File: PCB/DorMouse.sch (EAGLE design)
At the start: 46 parts, among them IC1 LM340MP-05, IC2 MAX1551, U1 STM32F10XRXT6, X1 MINI-USB-UX60-MB-5ST

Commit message: V1.1 Schematic update
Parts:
- removed JMP1, JMP2: 0R-JUMPA, jump-0r-smd:0R-JUMPA
- removed PAD1, PAD2, PAD3, PAD4: (no value), wirepad:SMD2
- added C21, C23, C24, C25: 0.1uF, rcl:C-EUC0402
- added CHRG: (no value), led:LEDCHIPLED_0603
- added GPS-LED, SD-LED, U$4: RED-GREEN_LED, DorMouse:RED-GREEN_LED
- added R10, R11, R12, R13, R14, R6, R9: 160, rcl:R-EU_R0402
- added R7: 10k, rcl:R-EU_R0402
- added S1, S2: (no value), SparkFun:TAC_SWITCHSMD
- BAROMETER: device DorMouse:MPL115A1 -> Swallow:MPL115A1
- C10: value 10nF -> 1uF
- C11: value 1uF -> 0.01uF
- C12, C7: value 0.1uF -> 0.01uF
- C13: value 0.1uF -> 10nF
- C14, C4: value 0.1uF -> 1uF
- GPS: device DorMouse:UBLOX_MAX-6 -> Swallow:UBLOX_MAX-6
- HIGH-G_ACC: device DorMouse:ADXL377 -> Swallow:ADXL377
- LOW-G_ACC: device DorMouse:ADXL345 -> Swallow:ADXL345
- XB1: device DorMouse:XBEE -> Swallow:XBEE
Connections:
- removed net AVR-INT0: GPS.4_TIMEPULSE
- removed net N$13: JMP2-0R.3, R4.1
- removed net N$22: JTAG1.7
- removed net N$25: JTAG1.9
- removed net U1-CTS: FTDI-HEADER.6, JMP1-0R.1
- removed net U1-RTS: FTDI-HEADER.2, JMP2-0R.1
- new net GENERAL_HAPPY_FACE: R14.2, U1PORTC_L.PC7
- new net GPS_:(: R9.2, U1PORTC_L.PC4
- new net GPS_:): R10.2, U1PORTC_L.PC3
- new net MISO-3: U1PORTB_L.PB4
- new net MOSI-3: U1PORTB_L.PB5
- new net N$17: GPS-LED.RED-ANODE, R9.1
- new net N$19: C10.1, FTDI-HEADER.6
- new net N$21: R7.2, U1PORTB_H.PB9
- new net N$27: GPS-LED.GREEN-ANODE, R10.1
- new net N$30: R11.1, SD-LED.RED-ANODE
- new net N$31: R12.1, SD-LED.GREEN-ANODE
- new net N$33: R13.1, U$4.RED-ANODE
- new net N$34: R14.1, U$4.GREEN-ANODE
- new net RESET: C10.2, C6.2, S2.1, S2.2, U1RESET.NRST
- new net SCK-3: U1PORTB_L.PB3
- new net SD-DET: CN1.CARD_DETECT, U1PORTC_H.PC13
- new net SD_:(: R11.2, U1PORTC_L.PC6
- new net SD_:): R12.2, U1PORTC_L.PC5
- new net SERGEANT_SAD_FACE: R13.2, U1PORTA_H.PA8
- new net TIMEPULSE: GPS.4_TIMEPULSE, U1PORTB_H.PB8
- net ADC1: now also C7.1
- net ADC2: now also C11.1
- net ADC3: now also C12.1
- net CHARGING(-): now also U1PORTA_L.PA0
- net GND: now also C12.2, C13.2, C14.2, C21.1, C23.1, C24.1, C25.1, C7.2, CN1.CARD_DETECT1, FTDI-HEADER.2, GPS-LED.CATHODE, JTAG1.9, R6.1, S2.3, S2.4, SD-LED.CATHODE, U$4.CATHODE, U1AN_POWER.VDDA; no longer C10.2, C12.1, C13.1, C14.1, PAD4.P, U1AN_POWER.VSSA
- net N$12: now also CHRG.C, R6.2; no longer JMP1-0R.3, R3.1
- net N$2: now also S1.3, S1.4; no longer PAD2.P
- net N$5: now also R3.1; no longer JMP1-0R.2
- net N$8: now also R4.1; no longer JMP2-0R.2
- net N$9: now also CHRG.A, U1PORTA_L.PA1; no longer C6.2, PAD3.P, U1RESET.NRST
- net TCK: no longer U1PORTA_H.PA14
- net TDI: no longer U1PORTA_H.PA15
- net TDO: no longer U1PORTB_L.PB3
- net TMS: no longer U1PORTA_H.PA13
- net USB-5V: now also R7.1
- net VCC: now also C13.1, C14.1, C21.2, C23.2, C24.2, C25.2, S1.1, S1.2, U1AN_POWER.VSSA; no longer C10.1, C11.1, C12.2, C13.2, C14.2, PAD1.P, U1AN_POWER.VDDA
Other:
- moved on the sheet: C10, C11, C12, C13, C14, C15, C16, C17, C18, C19, C20, C22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

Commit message: pcb v1
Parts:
- removed C13: 10nF, rcl:C-EUC0402
- removed C17, C20, C5: 0.1uF, rcl:C-EUC0402
- removed C4: 1uF, rcl:C-EUC0402
- added CN2: (no value), microbuilder:JST_2PINSH2
- renumbered U$4 to GENERAL
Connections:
- removed net NRESET: JTAG1.10
- removed net SCK-3: U1PORTB_L.PB3
- net GND: now also CN2.1; no longer C13.2, C17.1, C20.1, C4.1, C5.2
- net LIPO+: now also CN2.2; no longer C5.1
- net RESET: now also JTAG1.10
- net TCK: now also U1PORTA_H.PA14
- net TDI: now also U1PORTA_H.PA15
- net TDO: now also U1PORTB_L.PB3
- net TMS: now also U1PORTA_H.PA13
- net VCC: no longer C13.1, C17.2, C20.2, C4.2

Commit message: Multiple fixes to schematic, addition of pdf, clean board and partslist.
Ava library fixed: open and save, then it works (?)

Ran ERC: complained about missing joins and signals near each other without
being connected. Discovered one case where something that should be
conected was not. Fixed, then as a precautionary measure, added join
dots everywhere (sorry).

Wrong antenna footprint. Swapped.

Adam says the two-capacitors-with-different-values thing is to do with
response to different frequencies. Added datasheet recommended capacitor
values for the STM analogue.

Adjusted capacitor count for low g accel.

Add parts list
Add schematic PDF
Add 'clean, with groups of easy things routed' board.

Warning: I (foolishly) did the schematic modifications with the clean
board open. This de-synced the board, so I manually re synced them
afterwards, and eagle is now content. Hopefully crazy rubbish won't
happen.
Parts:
- removed C15: 0.1uF, rcl:C-EUC0402
- added C4: 10nF, rcl:C-EUC0402
- added C5: 4.7uF, rcl:C-EUC0402
- GPS: device Swallow:UBLOX_MAX-6 -> Ava:UBLOX_MAX-6
- U$1: value SARANTEL-SL1204 -> SARANTEL-SR1202; device Swallow:SARANTEL-SL1204 -> Ava:SARANTEL-SR1202
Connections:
- net GND: now also C4.2, C5.1, U1AN_POWER.VSSA; no longer C15.1, U1AN_POWER.VDDA
- net VCC: now also C4.1, C5.2, U1AN_POWER.VDDA; no longer C15.2, U1AN_POWER.VSSA
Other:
- moved on the sheet: C14, C16, C18, C19, C22, U1AN_POWER

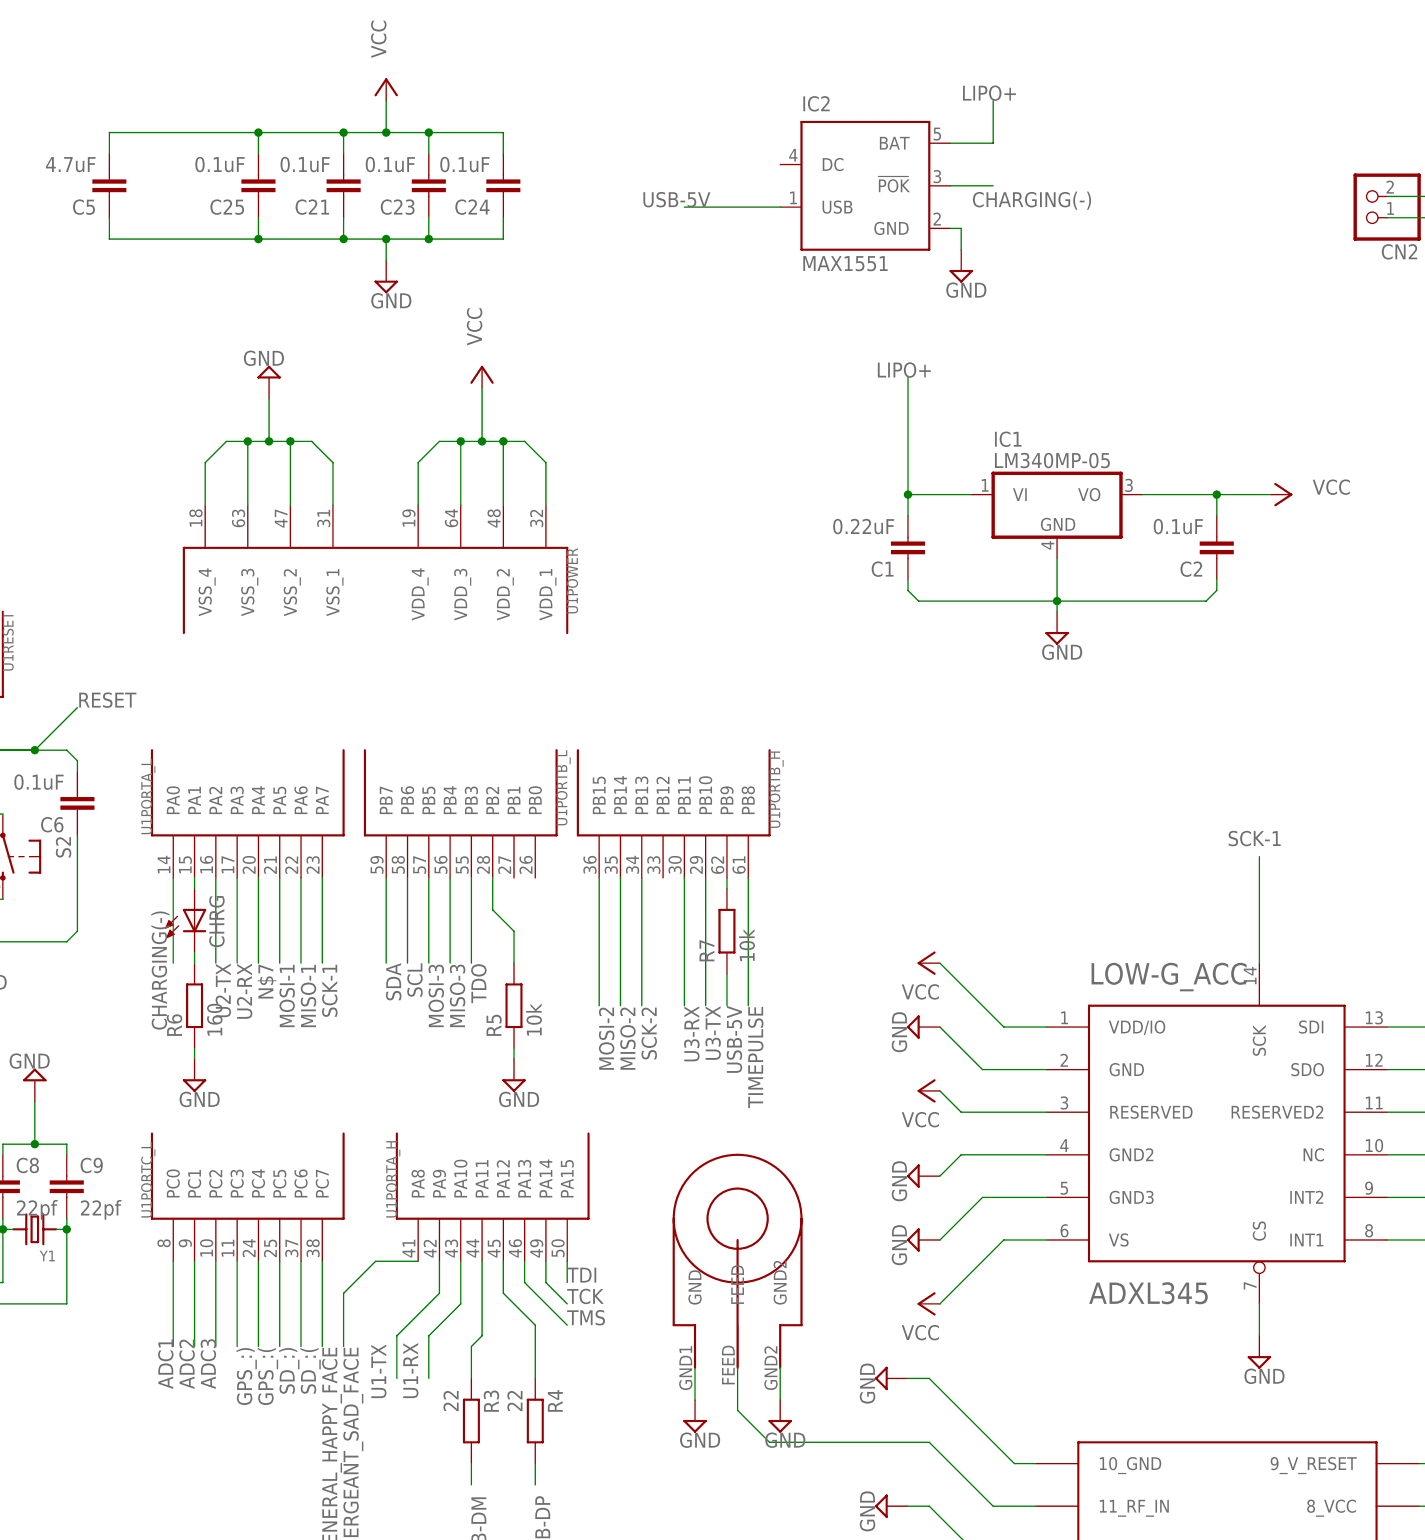
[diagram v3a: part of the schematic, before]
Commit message: Add resistor and cap, reverse ADC connections. Warning: desync
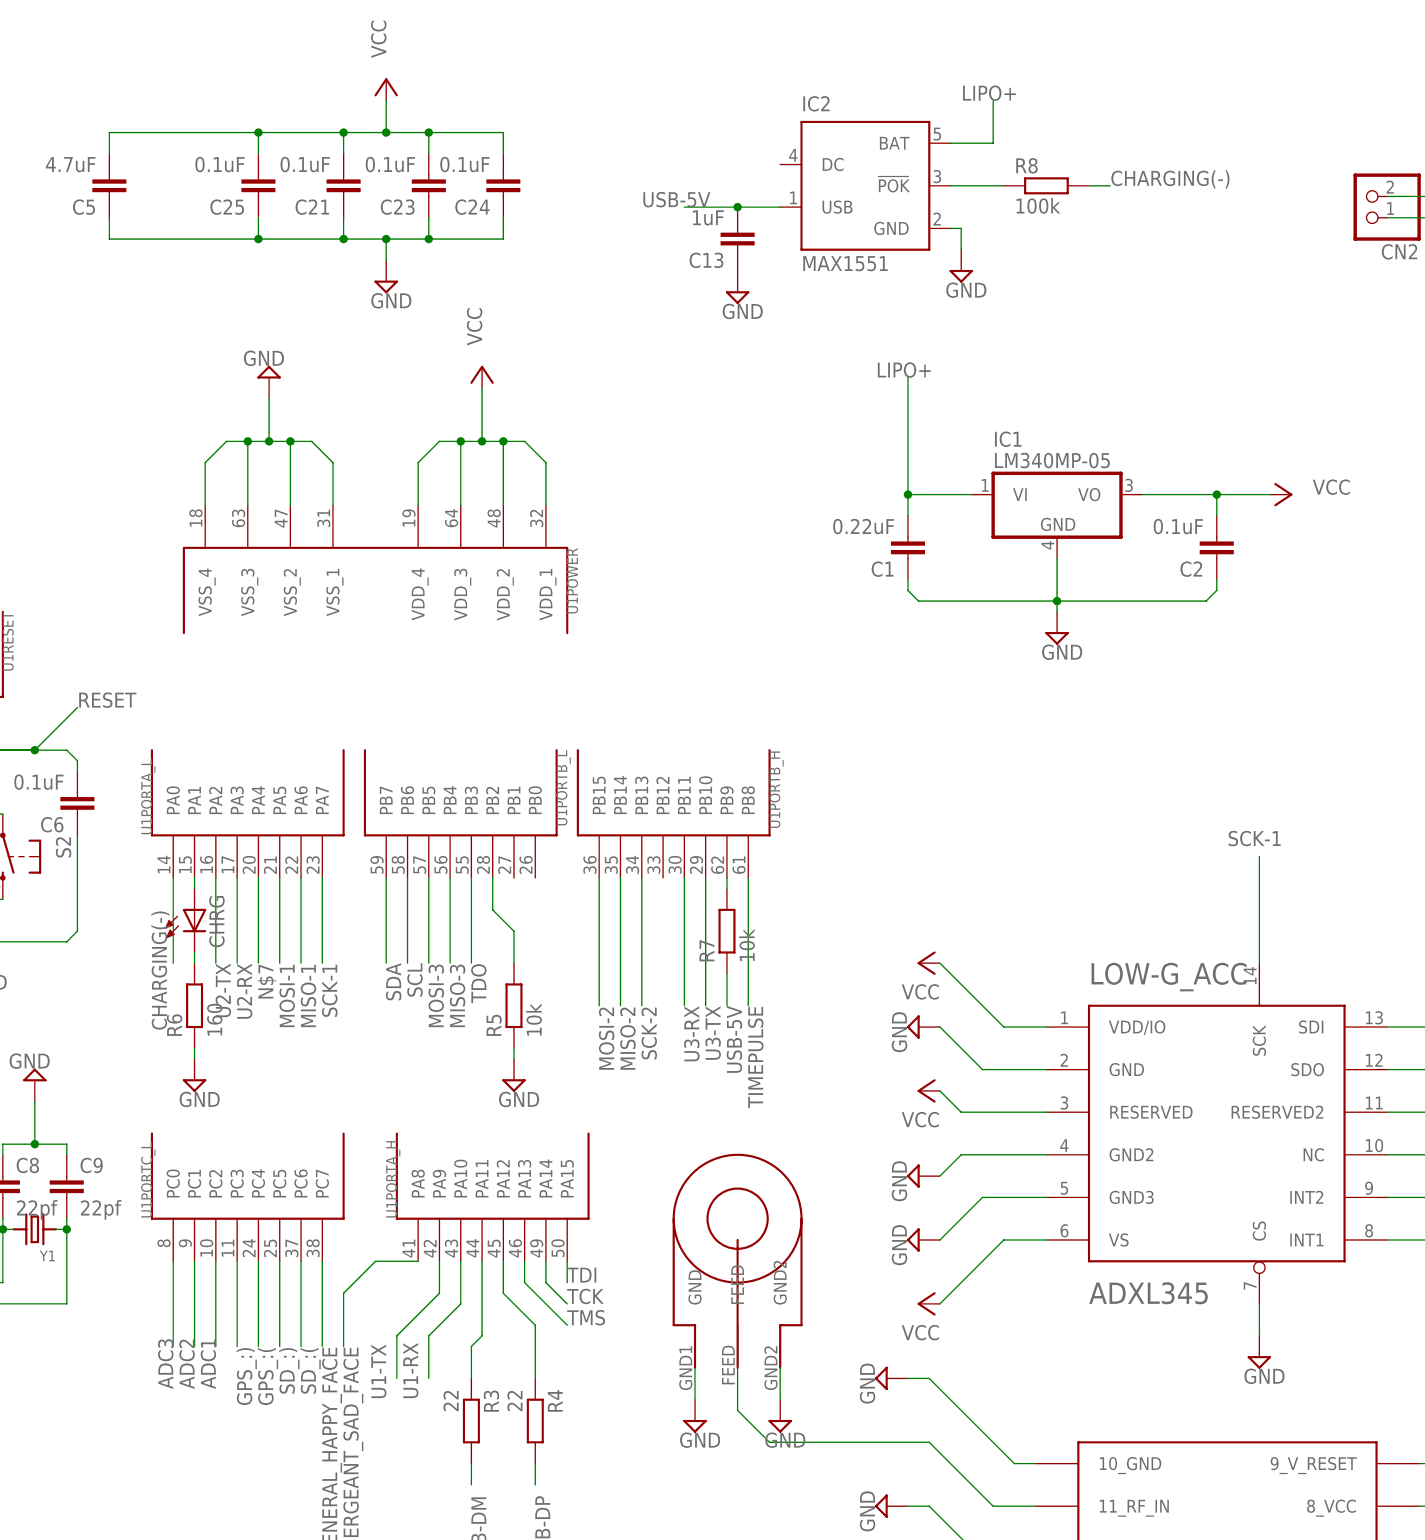
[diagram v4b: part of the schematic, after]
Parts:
- added C13: 1uF, rcl:C-EUC0402
- added R8: 100k, rcl:R-EU_R0402
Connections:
- new net N$13: IC2.!POK, R8.1
- net ADC1: now also U1PORTC_L.PC2; no longer U1PORTC_L.PC0
- net ADC3: now also U1PORTC_L.PC0; no longer U1PORTC_L.PC2
- net CHARGING(-): now also R8.2; no longer IC2.!POK
- net GND: now also C13.1
- net USB-5V: now also C13.2
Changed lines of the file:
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@@
 <part name="C4" library="rcl" deviceset="C-EU" device="C0402" value="10nF"/>
 <part name="C5" library="rcl" deviceset="C-EU" device="C0402" value="4.7uF"/>
+<part name="C13" library="rcl" deviceset="C-EU" device="C0402" value="1uF"/>
+<part name="SUPPLY11" library="supply2" deviceset="GND" device=""/>
+<part name="R8" library="rcl" deviceset="R-EU_" device="R0402" value="100k"/>
 </parts>
 <sheets>
@@
 <instance part="C4" gate="G$1" x="-168.91" y="80.01" rot="R180"/>
 <instance part="C5" gate="G$1" x="-85.09" y="121.92" rot="R180"/>
+<instance part="C13" gate="G$1" x="-10.16" y="115.57" rot="R180"/>
+<instance part="SUPPLY11" gate="GND" x="-10.16" y="110.49"/>
+<instance part="R8" gate="G$1" x="26.67" y="123.19"/>
 </instances>
 <busses>
@@
 <pinref part="SUPPLY41" gate="GND" pin="GND"/>
 </segment>
+<segment>
+<pinref part="C13" gate="G$1" pin="1"/>
+<pinref part="SUPPLY11" gate="GND" pin="GND"/>
+</segment>
 </net>
 <net name="VCC" class="0">
@@
 <segment>
 <pinref part="IC2" gate="G$1" pin="USB"/>
-<wire x1="-5.08" y1="120.65" x2="-16.51" y2="120.65" width="0.1524" layer="91"/>
+<wire x1="-5.08" y1="120.65" x2="-10.16" y2="120.65" width="0.1524" layer="91"/>
 <label x="-21.59" y="120.65" size="1.778" layer="95"/>
+<pinref part="C13" gate="G$1" pin="2"/>
+<wire x1="-10.16" y1="120.65" x2="-16.51" y2="120.65" width="0.1524" layer="91"/>
+<junction x="-10.16" y="120.65"/>
 </segment>
 <segment>
@@
 <net name="CHARGING(-)" class="0">
 <segment>
-<pinref part="IC2" gate="G$1" pin="!POK"/>
-<wire x1="15.24" y1="123.19" x2="20.32" y2="123.19" width="0.1524" layer="91"/>
-<label x="17.78" y="120.65" size="1.778" layer="95"/>
-</segment>
-<segment>
 <pinref part="U1" gate="PORTA_L" pin="PA0"/>
 <wire x1="-77.47" y1="40.64" x2="-77.47" y2="30.48" width="0.1524" layer="91"/>
 <label x="-80.01" y="36.83" size="1.778" layer="95" rot="R270"/>
+</segment>
+<segment>
+<pinref part="R8" gate="G$1" pin="2"/>
+<wire x1="31.75" y1="123.19" x2="34.29" y2="123.19" width="0.1524" layer="91"/>
+<label x="34.29" y="123.19" size="1.778" layer="95"/>
 </segment>
 </net>
@@
 <net name="ADC1" class="0">
 <segment>
-<wire x1="-77.47" y1="-5.08" x2="-77.47" y2="-15.24" width="0.1524" layer="91"/>
-<pinref part="U1" gate="PORTC_L" pin="PC0"/>
-<label x="-77.47" y="-20.32" size="1.778" layer="95" rot="R90"/>
-</segment>
-<segment>
 <pinref part="HIGH-G_ACC" gate="G$1" pin="Z_OUT"/>
 <wire x1="158.75" y1="25.4" x2="172.72" y2="25.4" width="0.1524" layer="91"/>
@@
 <pinref part="C7" gate="G$1" pin="1"/>
 </segment>
+<segment>
+<pinref part="U1" gate="PORTC_L" pin="PC2"/>
+<wire x1="-72.39" y1="-5.08" x2="-72.39" y2="-15.24" width="0.1524" layer="91"/>
+<label x="-72.39" y="-20.32" size="1.778" layer="95" rot="R90"/>
+</segment>
 </net>
 <net name="ADC2" class="0">
-<segment>
-<pinref part="U1" gate="PORTC_L" pin="PC1"/>
-<wire x1="-74.93" y1="-5.08" x2="-74.93" y2="-15.24" width="0.1524" layer="91"/>
-<label x="-74.93" y="-20.32" size="1.778" layer="95" rot="R90"/>
-</segment>
 <segment>
 <pinref part="HIGH-G_ACC" gate="G$1" pin="Y_OUT"/>
@@
 <pinref part="C11" gate="G$1" pin="1"/>
 </segment>
+<segment>
+<pinref part="U1" gate="PORTC_L" pin="PC1"/>
+<wire x1="-74.93" y1="-5.08" x2="-74.93" y2="-15.24" width="0.1524" layer="91"/>
+<label x="-74.93" y="-20.32" size="1.778" layer="95" rot="R90"/>
+</segment>
 </net>
 <net name="ADC3" class="0">
-<segment>
-<pinref part="U1" gate="PORTC_L" pin="PC2"/>
-<wire x1="-72.39" y1="-5.08" x2="-72.39" y2="-15.24" width="0.1524" layer="91"/>
-<label x="-72.39" y="-20.32" size="1.778" layer="95" rot="R90"/>
-</segment>
 <segment>
 <pinref part="HIGH-G_ACC" gate="G$1" pin="X_OUT"/>
@@
 <label x="165.1" y="15.24" size="1.778" layer="95"/>
 <pinref part="C12" gate="G$1" pin="1"/>
+</segment>
+<segment>
+<wire x1="-77.47" y1="-5.08" x2="-77.47" y2="-15.24" width="0.1524" layer="91"/>
+<pinref part="U1" gate="PORTC_L" pin="PC0"/>
+<label x="-77.47" y="-20.32" size="1.778" layer="95" rot="R90"/>
 </segment>
 </net>
@@
 </segment>
 </net>
+<net name="N$13" class="0">
+<segment>
+<pinref part="IC2" gate="G$1" pin="!POK"/>
+<pinref part="R8" gate="G$1" pin="1"/>
+<wire x1="21.59" y1="123.19" x2="15.24" y2="123.19" width="0.1524" layer="91"/>
+</segment>
+</net>

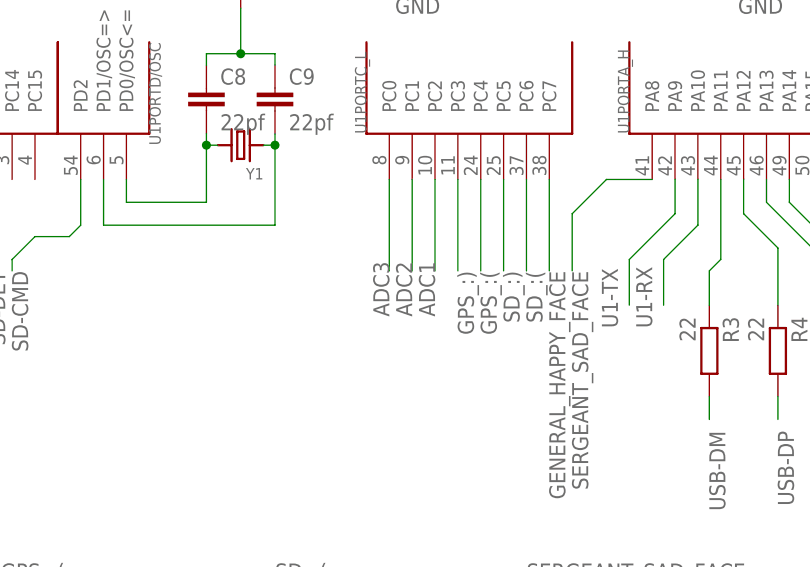
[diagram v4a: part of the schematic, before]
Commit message: Sync older board with schematic
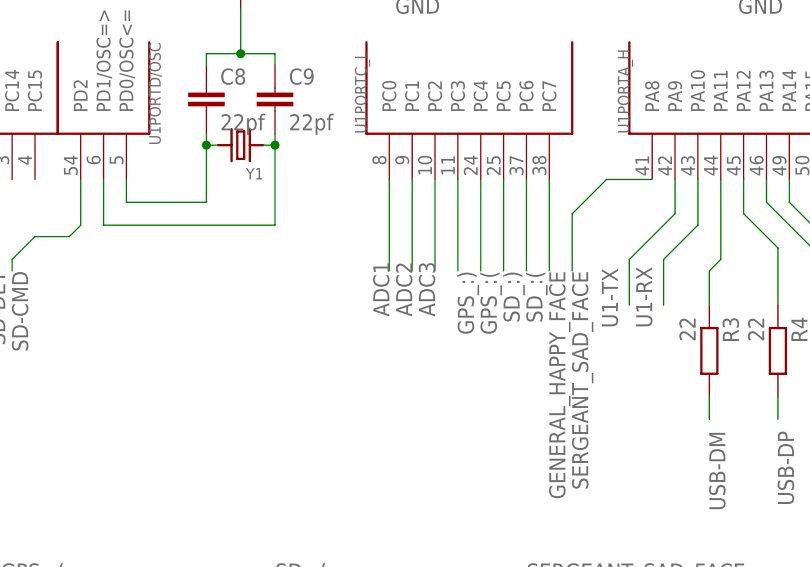
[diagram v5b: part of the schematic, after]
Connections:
- net ADC1: now also U1PORTC_L.PC0; no longer U1PORTC_L.PC2
- net ADC3: now also U1PORTC_L.PC2; no longer U1PORTC_L.PC0
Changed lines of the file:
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@@
 <setting verticaltext="up"/>
 </settings>
-<grid distance="0.05" unitdist="inch" unit="inch" style="lines" multiple="1" display="no" altdistance="0.01" altunitdist="inch" altunit="inch"/>
+<grid distance="0.1" unitdist="inch" unit="inch" style="lines" multiple="1" display="no" altdistance="0.01" altunitdist="inch" altunit="inch"/>
 <layers>
 <layer number="1" name="Top" color="4" fill="1" visible="no" active="no"/>
@@
 </segment>
 <segment>
-<pinref part="U1" gate="PORTC_L" pin="PC2"/>
-<wire x1="-72.39" y1="-5.08" x2="-72.39" y2="-15.24" width="0.1524" layer="91"/>
-<label x="-72.39" y="-20.32" size="1.778" layer="95" rot="R90"/>
+<wire x1="-77.47" y1="-5.08" x2="-77.47" y2="-15.24" width="0.1524" layer="91"/>
+<pinref part="U1" gate="PORTC_L" pin="PC0"/>
+<label x="-77.47" y="-20.32" size="1.778" layer="95" rot="R90"/>
 </segment>
 </net>
@@
 </segment>
 <segment>
-<wire x1="-77.47" y1="-5.08" x2="-77.47" y2="-15.24" width="0.1524" layer="91"/>
-<pinref part="U1" gate="PORTC_L" pin="PC0"/>
-<label x="-77.47" y="-20.32" size="1.778" layer="95" rot="R90"/>
-</segment>
-</net>
+<pinref part="U1" gate="PORTC_L" pin="PC2"/>
+<wire x1="-72.39" y1="-5.08" x2="-72.39" y2="-15.24" width="0.1524" layer="91"/>
+<label x="-72.39" y="-20.32" size="1.778" layer="95" rot="R90"/>
+</segment>
+</net>
